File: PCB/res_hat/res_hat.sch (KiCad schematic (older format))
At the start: 55 parts, among them IC1 MCP4725A0T-E_CH, IC2 MCP4725A0T-E_CH, IC3 UCC27324D, J1 Conn_02x20_Odd_Even, J10 Conn_01x02, J11 Jack-DC, J2 Conn_02x04_Odd_Even, J3 Conn_01x03, J4 Conn_01x06, J5 Conn_Coaxial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

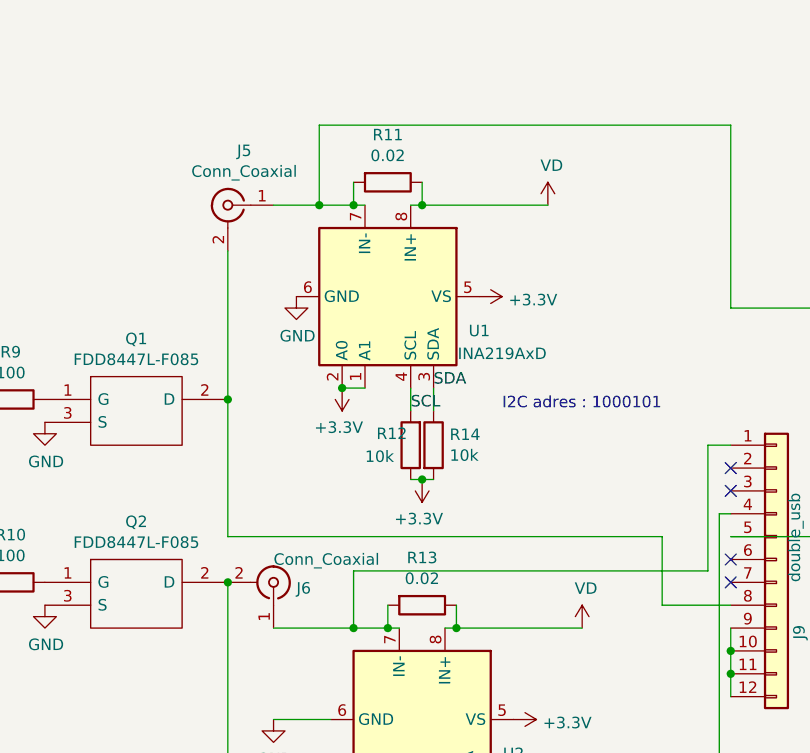
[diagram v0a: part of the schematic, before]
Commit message: update/add LCSC ref and create fab file
bug for Res_hat with JLCPCB site
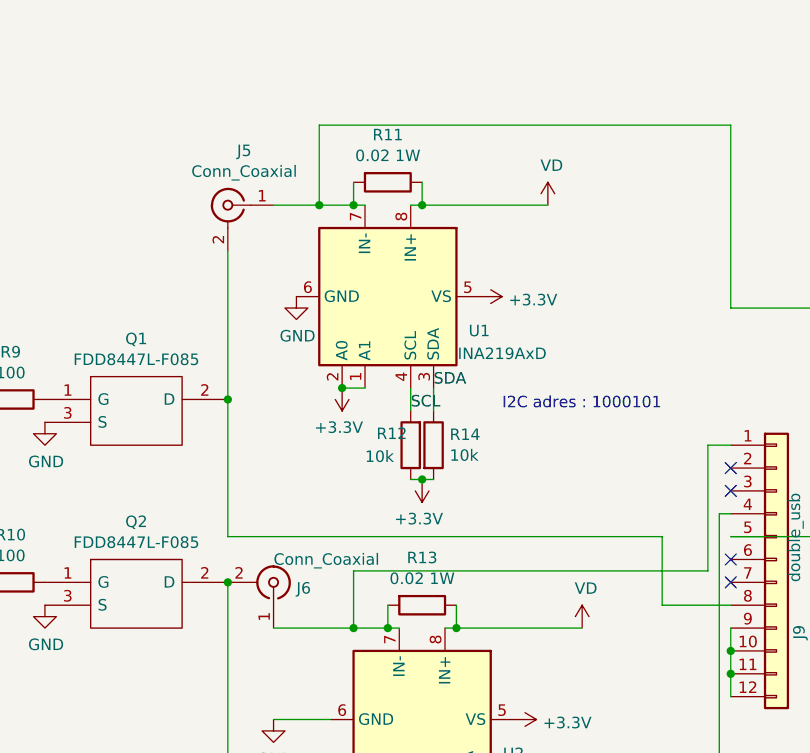
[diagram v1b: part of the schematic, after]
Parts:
- C1, C3: LCSC (none) -> C15850
- C2, C4, C5: LCSC (none) -> C49678
- C6: LCSC (none) -> C28323
- IC1, IC2: LCSC (none) -> C144198
- IC3: LCSC (none) -> C46427
- Q1, Q2: LCSC (none) -> C99591
- R1, R12, R14, R16, R17, R2, R3, R4, R5, R6, R7, R8, R9: LCSC (none) -> C17414
- R10: LCSC (none) -> C17408
- R11, R13: value 0.02 -> 0.02 1W; footprint Resistor_SMD:R_2010_5025Metric -> Resistor_SMD:R_2512_6332Metric; LCSC (none) -> C127705
- R15: LCSC (none) -> C17673
- U1, U2: LCSC (none) -> C138706
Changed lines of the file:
@@
 F 8 "Microchip" H 6600 1950 50  0001 L CNN "Manufacturer_Name"
 F 9 "MCP4725A0T-E/CH" H 6600 1850 50  0001 L CNN "Manufacturer_Part_Number"
+F 10 "C144198" H 5650 2450 50  0001 C CNN "LCSC"
 	1    5650 2450
 	-1   0    0    1
@@
 F 8 "Microchip" H 6600 2900 50  0001 L CNN "Manufacturer_Name"
 F 9 "MCP4725A0T-E/CH" H 6600 2800 50  0001 L CNN "Manufacturer_Part_Number"
+F 10 "C144198" H 5650 3400 50  0001 C CNN "LCSC"
 	1    5650 3400
 	-1   0    0    1
@@
 F 8 "Texas Instruments" H 7100 2000 50  0001 L CNN "Manufacturer_Name"
 F 9 "UCC27324D" H 7100 1900 50  0001 L CNN "Manufacturer_Part_Number"
+F 10 "C46427" H 6050 2500 50  0001 C CNN "LCSC"
 	1    6050 2500
 	1    0    0    -1
@@
 F 8 "ON Semiconductor" H 8450 1750 50  0001 L CNN "Manufacturer_Name"
 F 9 "FDD8447L-F085" H 8450 1650 50  0001 L CNN "Manufacturer_Part_Number"
+F 10 "C99591" H 7800 2250 50  0001 C CNN "LCSC"
 	1    7800 2250
 	1    0    0    -1
@@
 F 8 "ON Semiconductor" H 8450 2550 50  0001 L CNN "Manufacturer_Name"
 F 9 "FDD8447L-F085" H 8450 2450 50  0001 L CNN "Manufacturer_Part_Number"
+F 10 "C99591" H 7800 3050 50  0001 C CNN "LCSC"
 	1    7800 3050
 	1    0    0    -1
@@
 F 2 "Package_SO:SOIC-8_3.9x4.9mm_P1.27mm" H 10250 3300 50  0001 C CNN
 F 3 "http://www.ti.com/lit/ds/symlink/ina219.pdf" H 9800 3550 50  0001 C CNN
+F 4 "C138706" V 9450 3650 50  0001 C CNN "LCSC"
 	1    9450 3650
 	0    1    1    0
@@
 P 9450 3150
 F 0 "R13" V 9243 3150 50  0000 C CNN
-F 1 "0.02" V 9334 3150 50  0000 C CNN
-F 2 "Resistor_SMD:R_2010_5025Metric" V 9380 3150 50  0001 C CNN
+F 1 "0.02 1W" V 9334 3150 50  0000 C CNN
+F 2 "Resistor_SMD:R_2512_6332Metric" V 9380 3150 50  0001 C CNN
 F 3 "~" H 9450 3150 50  0001 C CNN
+F 4 "C127705" V 9450 3150 50  0001 C CNN "LCSC"
 	1    9450 3150
 	0    1    1    0
@@
 F 2 "Resistor_SMD:R_0805_2012Metric" V 9580 4300 50  0001 C CNN
 F 3 "~" H 9650 4300 50  0001 C CNN
+F 4 "C17414" H 9650 4300 50  0001 C CNN "LCSC"
 	1    9650 4300
 	1    0    0    -1
@@
 F 2 "Resistor_SMD:R_0805_2012Metric" V 9480 4300 50  0001 C CNN
 F 3 "~" H 9550 4300 50  0001 C CNN
+F 4 "C17414" H 9550 4300 50  0001 C CNN "LCSC"
 	1    9550 4300
 	-1   0    0    1
@@
 F 2 "Package_SO:SOIC-8_3.9x4.9mm_P1.27mm" H 10100 1450 50  0001 C CNN
 F 3 "http://www.ti.com/lit/ds/symlink/ina219.pdf" H 9650 1700 50  0001 C CNN
+F 4 "C138706" V 9300 1800 50  0001 C CNN "LCSC"
 	1    9300 1800
 	0    1    1    0
@@
 P 9300 1300
 F 0 "R11" V 9093 1300 50  0000 C CNN
-F 1 "0.02" V 9184 1300 50  0000 C CNN
-F 2 "Resistor_SMD:R_2010_5025Metric" V 9230 1300 50  0001 C CNN
+F 1 "0.02 1W" V 9184 1300 50  0000 C CNN
+F 2 "Resistor_SMD:R_2512_6332Metric" V 9230 1300 50  0001 C CNN
 F 3 "~" H 9300 1300 50  0001 C CNN
+F 4 "C127705" V 9300 1300 50  0001 C CNN "LCSC"
 	1    9300 1300
 	0    1    1    0
@@
 F 2 "Resistor_SMD:R_0805_2012Metric" V 9430 2450 50  0001 C CNN
 F 3 "~" H 9500 2450 50  0001 C CNN
+F 4 "C17414" H 9500 2450 50  0001 C CNN "LCSC"
 	1    9500 2450
 	1    0    0    -1
@@
 F 2 "Resistor_SMD:R_0805_2012Metric" V 9330 2450 50  0001 C CNN
 F 3 "~" H 9400 2450 50  0001 C CNN
+F 4 "C17414" H 9400 2450 50  0001 C CNN "LCSC"
 	1    9400 2450
 	-1   0    0    1
@@
 F 2 "Resistor_SMD:R_0805_2012Metric" V 7580 2250 50  0001 C CNN
 F 3 "~" H 7650 2250 50  0001 C CNN
+F 4 "C17414" V 7650 2250 50  0001 C CNN "LCSC"
 	1    7650 2250
 	0    1    1    0
@@
 F 2 "Resistor_SMD:R_0805_2012Metric" V 7580 3050 50  0001 C CNN
 F 3 "~" H 7650 3050 50  0001 C CNN
+F 4 "C17408" V 7650 3050 50  0001 C CNN "LCSC"
 	1    7650 3050
 	0    1    1    0
@@
 F 2 "Resistor_SMD:R_0805_2012Metric" V 7430 1800 50  0001 C CNN
 F 3 "~" H 7500 1800 50  0001 C CNN
+F 4 "C17414" V 7500 1800 50  0001 C CNN "LCSC"
 	1    7500 1800
 	1    0    0    -1
@@
 F 2 "Resistor_SMD:R_0805_2012Metric" V 7430 3500 50  0001 C CNN
 F 3 "~" H 7500 3500 50  0001 C CNN
+F 4 "C17414" V 7500 3500 50  0001 C CNN "LCSC"
 	1    7500 3500
 	1    0    0    -1
@@
 F 2 "Resistor_SMD:R_0805_2012Metric" V 5880 2000 50  0001 C CNN
 F 3 "~" H 5950 2000 50  0001 C CNN
+F 4 "C17414" H 5950 2000 50  0001 C CNN "LCSC"
 	1    5950 2000
 	1    0    0    -1
@@
 F 2 "Resistor_SMD:R_0805_2012Metric" V 5780 3550 50  0001 C CNN
 F 3 "~" H 5850 3550 50  0001 C CNN
+F 4 "C17414" H 5850 3550 50  0001 C CNN "LCSC"
 	1    5850 3550
 	1    0    0    -1
@@
 F 2 "Resistor_SMD:R_0805_2012Metric" V 4480 2000 50  0001 C CNN
 F 3 "~" H 4550 2000 50  0001 C CNN
+F 4 "C17414" H 4550 2000 50  0001 C CNN "LCSC"
 	1    4550 2000
 	1    0    0    -1
@@
 F 2 "Resistor_SMD:R_0805_2012Metric" V 4230 2000 50  0001 C CNN
 F 3 "~" H 4300 2000 50  0001 C CNN
+F 4 "C17414" H 4300 2000 50  0001 C CNN "LCSC"
 	1    4300 2000
 	1    0    0    -1
@@
 F 2 "Resistor_SMD:R_0805_2012Metric" V 4480 2950 50  0001 C CNN
 F 3 "~" H 4550 2950 50  0001 C CNN
+F 4 "C17414" H 4550 2950 50  0001 C CNN "LCSC"
 	1    4550 2950
 	1    0    0    -1
@@
 F 2 "Resistor_SMD:R_0805_2012Metric" V 4230 2950 50  0001 C CNN
 F 3 "~" H 4300 2950 50  0001 C CNN
+F 4 "C17414" H 4300 2950 50  0001 C CNN "LCSC"
 	1    4300 2950
 	1    0    0    -1
@@
 F 2 "Capacitor_SMD:C_0805_2012Metric" H 7238 2850 50  0001 C CNN
 F 3 "~" H 7200 3000 50  0001 C CNN
+F 4 "C49678" V 7200 3000 50  0001 C CNN "LCSC"
 	1    7200 3000
 	0    1    1    0
@@
 F 2 "Capacitor_SMD:C_0805_2012Metric" H 7238 3050 50  0001 C CNN
 F 3 "~" H 7200 3200 50  0001 C CNN
+F 4 "C28323" V 7200 3200 50  0001 C CNN "LCSC"
 	1    7200 3200
 	0    1    1    0
@@
 F 2 "Capacitor_SMD:C_0805_2012Metric" H 5538 1750 50  0001 C CNN
 F 3 "~" H 5500 1900 50  0001 C CNN
+F 4 "C49678" V 5500 1900 50  0001 C CNN "LCSC"
 	1    5500 1900
 	0    -1   -1   0
@@
 F 2 "Capacitor_SMD:C_0805_2012Metric" H 5538 1550 50  0001 C CNN
 F 3 "~" H 5500 1700 50  0001 C CNN
+F 4 "C15850" V 5500 1700 50  0001 C CNN "LCSC"
 	1    5500 1700
 	0    -1   -1   0
@@
 F 2 "Capacitor_SMD:C_0805_2012Metric" H 5538 2850 50  0001 C CNN
 F 3 "~" H 5500 3000 50  0001 C CNN
+F 4 "C49678" V 5500 3000 50  0001 C CNN "LCSC"
 	1    5500 3000
 	0    -1   -1   0
@@
 F 2 "Capacitor_SMD:C_0805_2012Metric" H 5538 2650 50  0001 C CNN
 F 3 "~" H 5500 2800 50  0001 C CNN
+F 4 "C15850" V 5500 2800 50  0001 C CNN "LCSC"
 	1    5500 2800
 	0    -1   -1   0
@@
 F 2 "Resistor_SMD:R_0805_2012Metric" V 9430 5550 50  0001 C CNN
 F 3 "~" H 9500 5550 50  0001 C CNN
+F 4 "C17673" V 9500 5550 50  0001 C CNN "LCSC"
 	1    9500 5550
 	0    1    1    0
